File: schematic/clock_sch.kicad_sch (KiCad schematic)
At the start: 7 parts

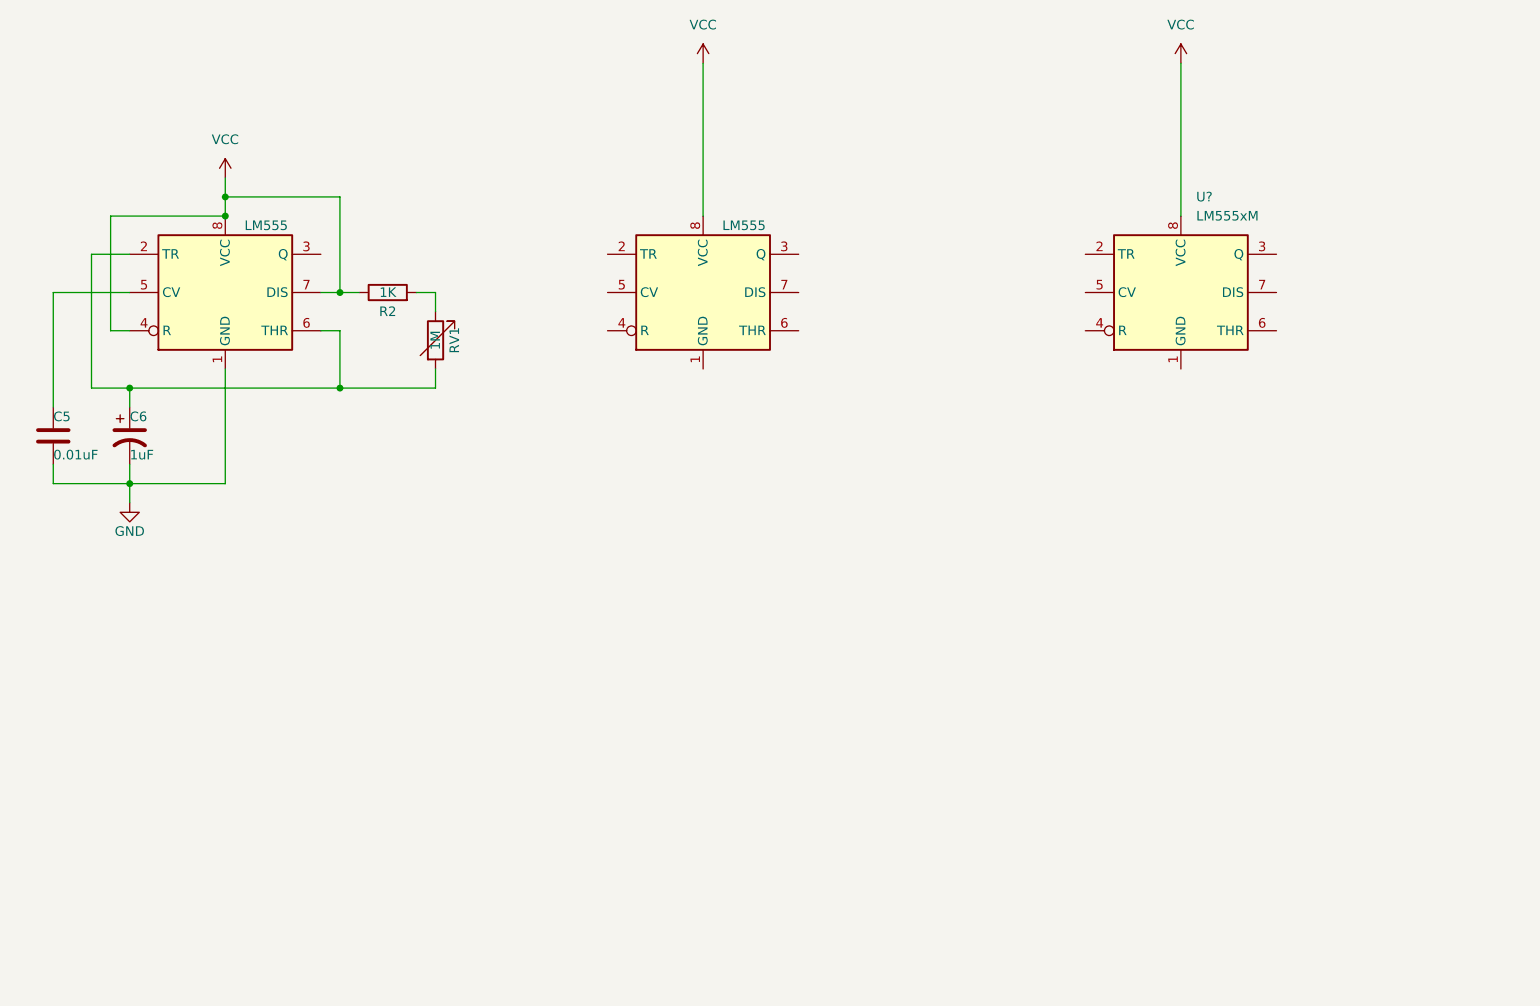
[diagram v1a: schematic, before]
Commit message: Added label and box
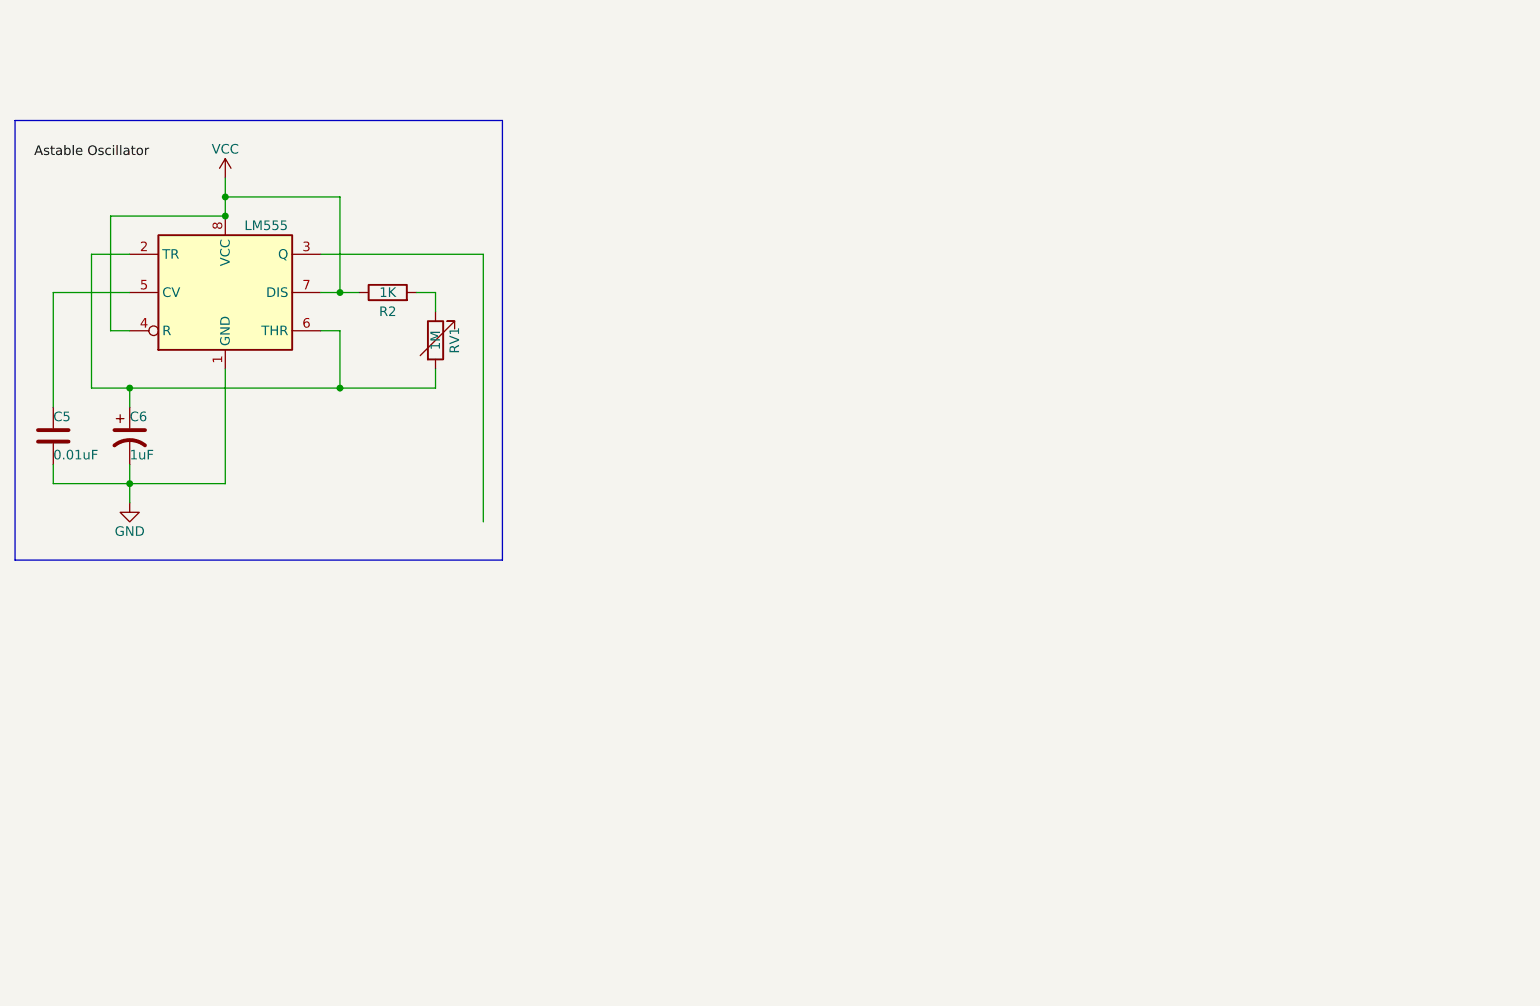
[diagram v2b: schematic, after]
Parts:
- removed U?: LM555, Package_SO:SOIC-8_3.9x4.9mm_P1.27mm, symbol Timer:LM555xM
- removed U?: LM555xM, Package_SO:SOIC-8_3.9x4.9mm_P1.27mm, symbol Timer:LM555xM
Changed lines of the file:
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@@
   (junction (at 50.8 96.52) (diameter 0) (color 0 0 0 0)
+  )
+  (wire (pts (xy 97.79 66.04) (xy 97.79 101.6))
+    (stroke (width 0) (type default) (color 0 0 0 0))
   )
   (wire (pts (xy 63.5 60.96) (xy 48.26 60.96))
@@
     (stroke (width 0) (type default) (color 0 0 0 0))
   )
-  (wire (pts (xy 190.5 40.64) (xy 190.5 60.96))
+  (polyline (pts (xy 100.33 106.68) (xy 100.33 48.26))
+    (stroke (width 0) (type default) (color 0 0 0 0))
+  )
+  (polyline (pts (xy 35.56 48.26) (xy 100.33 48.26))
     (stroke (width 0) (type default) (color 0 0 0 0))
   )
@@
     (stroke (width 0) (type default) (color 0 0 0 0))
   )
+  (polyline (pts (xy 35.56 106.68) (xy 100.33 106.68))
+    (stroke (width 0) (type default) (color 0 0 0 0))
+  )
   (wire (pts (xy 76.2 76.2) (xy 78.74 76.2))
+    (stroke (width 0) (type default) (color 0 0 0 0))
+  )
+  (polyline (pts (xy 35.56 48.26) (xy 35.56 106.68))
     (stroke (width 0) (type default) (color 0 0 0 0))
   )
@@
   )
   (wire (pts (xy 63.5 58.42) (xy 78.74 58.42))
-    (stroke (width 0) (type default) (color 0 0 0 0))
-  )
-  (wire (pts (xy 127 40.64) (xy 127 60.96))
     (stroke (width 0) (type default) (color 0 0 0 0))
   )
@@
     (stroke (width 0) (type default) (color 0 0 0 0))
   )
-  (symbol (lib_id "Timer:LM555xM") (at 127 71.12 0) (unit 1)
-    (in_bom yes) (on_board yes)
-    (property "Reference" "U?" (id 0) (at 129.0194 58.42 0)
-      (effects (font (size 1.27 1.27)) (justify left) hide)
-    )
-    (property "Value" "LM555" (id 1) (at 129.54 62.23 0)
-      (effects (font (size 1.27 1.27)) (justify left))
-    )
-    (property "Footprint" "Package_SO:SOIC-8_3.9x4.9mm_P1.27mm" (id 2) (at 148.59 81.28 0)
-      (effects (font (size 1.27 1.27)) hide)
-    )
-    (property "Datasheet" "http://www.ti.com/lit/ds/symlink/lm555.pdf" (id 3) (at 148.59 81.28 0)
-      (effects (font (size 1.27 1.27)) hide)
-    )
-    (pin "1")
-    (pin "8")
-    (pin "2")
-    (pin "3")
-    (pin "4")
-    (pin "5")
-    (pin "6")
-    (pin "7")
+  (wire (pts (xy 76.2 66.04) (xy 97.79 66.04))
+    (stroke (width 0) (type default) (color 0 0 0 0))
+  )
+  (label "Astable Oscillator" (at 38.1 53.34 0)
+    (effects (font (size 1.27 1.27)) (justify left bottom))
   )
   (symbol (lib_id "Timer:LM555xM") (at 63.5 71.12 0) (unit 1)
@@
     (pin "6")
     (pin "7")
-  )
-  (symbol (lib_id "Timer:LM555xM") (at 190.5 71.12 0) (unit 1)
-    (in_bom yes) (on_board yes) (fields_autoplaced)
-    (property "Reference" "U?" (id 0) (at 192.5194 58.42 0)
-      (effects (font (size 1.27 1.27)) (justify left))
-    )
-    (property "Value" "LM555xM" (id 1) (at 192.5194 60.96 0)
-      (effects (font (size 1.27 1.27)) (justify left))
-    )
-    (property "Footprint" "Package_SO:SOIC-8_3.9x4.9mm_P1.27mm" (id 2) (at 212.09 81.28 0)
-      (effects (font (size 1.27 1.27)) hide)
-    )
-    (property "Datasheet" "http://www.ti.com/lit/ds/symlink/lm555.pdf" (id 3) (at 212.09 81.28 0)
-      (effects (font (size 1.27 1.27)) hide)
-    )
-    (pin "1")
-    (pin "8")
-    (pin "2")
-    (pin "3")
-    (pin "4")
-    (pin "5")
-    (pin "6")
-    (pin "7")
-  )
-  (symbol (lib_id "power:VCC") (at 190.5 40.64 0) (unit 1)
-    (in_bom yes) (on_board yes) (fields_autoplaced)
-    (property "Reference" "#PWR?" (id 0) (at 190.5 44.45 0)
-      (effects (font (size 1.27 1.27)) hide)
-    )
-    (property "Value" "VCC" (id 1) (at 190.5 35.56 0))
-    (property "Footprint" "" (id 2) (at 190.5 40.64 0)
-      (effects (font (size 1.27 1.27)) hide)
-    )
-    (property "Datasheet" "" (id 3) (at 190.5 40.64 0)
-      (effects (font (size 1.27 1.27)) hide)
-    )
-    (pin "1")
-  )
-  (symbol (lib_id "power:VCC") (at 127 40.64 0) (unit 1)
-    (in_bom yes) (on_board yes) (fields_autoplaced)
-    (property "Reference" "#PWR?" (id 0) (at 127 44.45 0)
-      (effects (font (size 1.27 1.27)) hide)
-    )
-    (property "Value" "VCC" (id 1) (at 127 35.56 0))
-    (property "Footprint" "" (id 2) (at 127 40.64 0)
-      (effects (font (size 1.27 1.27)) hide)
-    )
-    (property "Datasheet" "" (id 3) (at 127 40.64 0)
-      (effects (font (size 1.27 1.27)) hide)
-    )
-    (pin "1")
   )
   (symbol (lib_id "Device:R_Variable") (at 91.44 77.47 0) (unit 1)
@@
   )
   (symbol (lib_id "power:VCC") (at 63.5 55.88 0) (unit 1)
-    (in_bom yes) (on_board yes) (fields_autoplaced)
+    (in_bom yes) (on_board yes)
     (property "Reference" "#PWR?" (id 0) (at 63.5 59.69 0)
       (effects (font (size 1.27 1.27)) hide)
     )
-    (property "Value" "VCC" (id 1) (at 63.5 50.8 0))
+    (property "Value" "VCC" (id 1) (at 63.5 52.07 0))
     (property "Footprint" "" (id 2) (at 63.5 55.88 0)
       (effects (font (size 1.27 1.27)) hide)

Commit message: dded Monostable oscillator and mode selection circuits
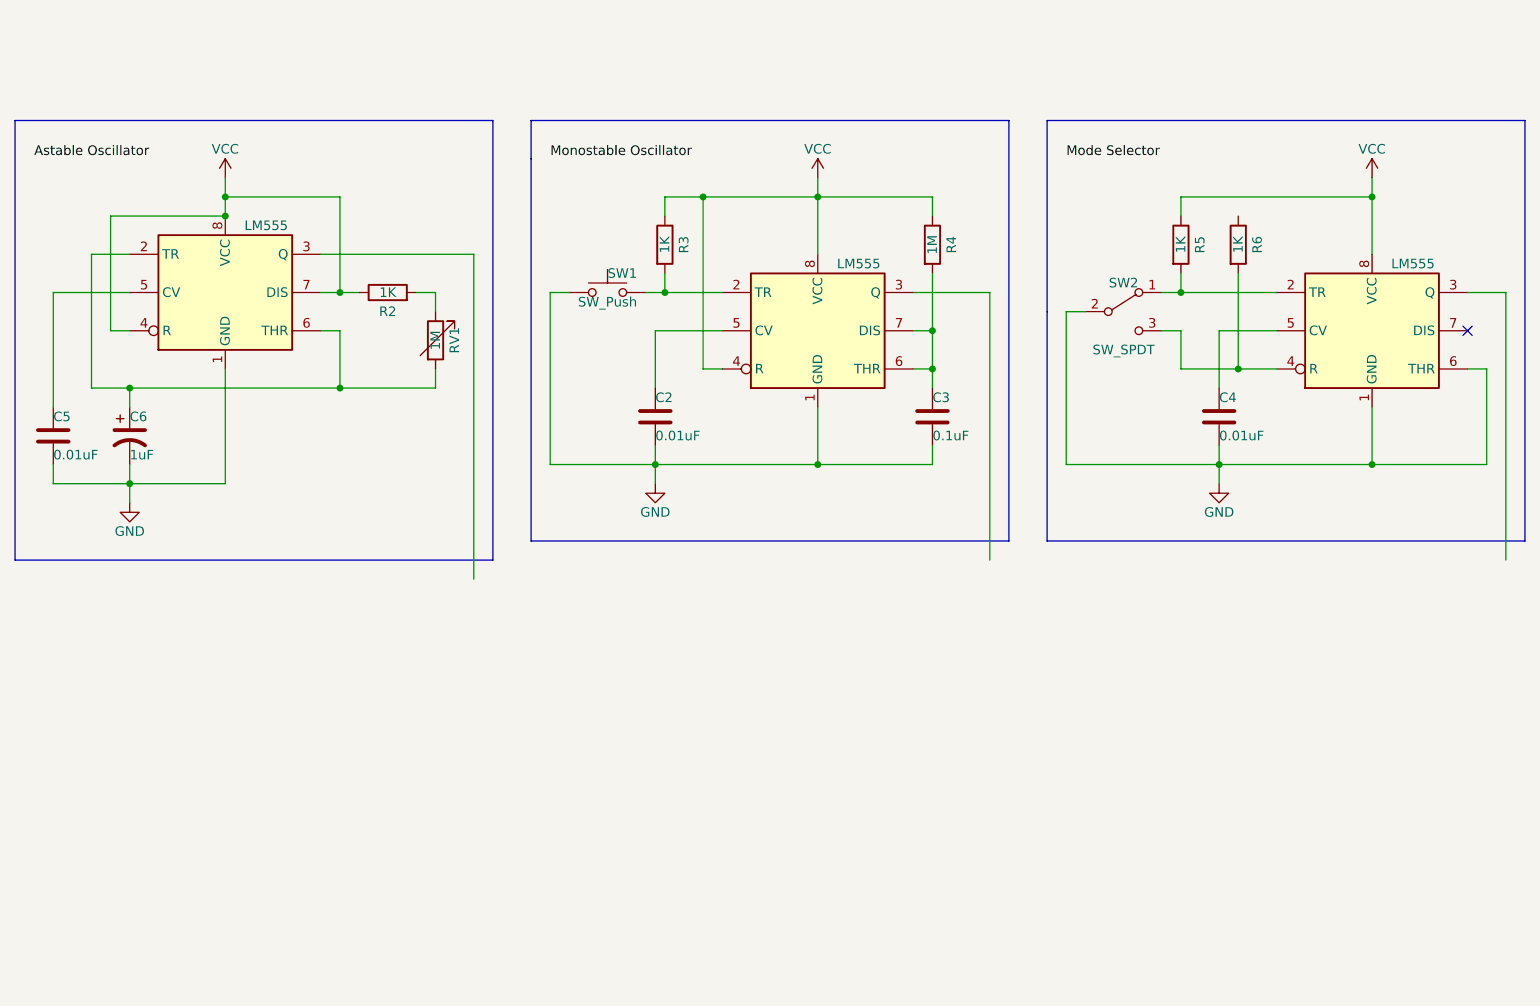
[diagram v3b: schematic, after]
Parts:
- added C2, C4: 0.01uF, symbol Device:C
- added C3: 0.1uF, symbol Device:C
- added R3, R5, R6: 1K, symbol Device:R
- added R4: 1M, symbol Device:R
- added SW1: SW_Push, symbol Switch:SW_Push
- added SW2: SW_SPDT, symbol Switch:SW_SPDT
- added U? (x2): LM555, Package_SO:SOIC-8_3.9x4.9mm_P1.27mm, symbol Timer:LM555xM
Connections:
- net GND: now also C2.2, C3.2, C4.2, SW1.1, SW2.2 (B), U?.1 (GND), U?.1 (GND), U?.6 (THR)
- net VCC: now also R3.1, R4.1, R5.1, U?.4 (R), U?.8 (VCC), U?.8 (VCC)
- new net: C2.1, U?.5 (CV)
- new net: R3.2, SW1.2, U?.2 (TR)
- new net: C4.1, U?.5 (CV)
- new net: R5.2, SW2.1 (A), U?.2 (TR)
- new net: R6.2, SW2.3 (C), U?.4 (R)
- new net: C3.1, R4.2, U?.6 (THR), U?.7 (DIS)
- no-connect marks 0 -> 1

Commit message: Implemented switching logic
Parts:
- added U4: 74LS04, symbol 74xx:74LS04
- added U5: 74LS08, symbol 74xx:74LS08
- added U6: 74LS32, symbol 74xx:74LS32
- gave numbers to parts that had none: 3
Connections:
- new net: U4.13, U5.8
- new net: U4.2, U5.4
- new net: U5.6, U6.2
- new net: U5.3, U6.1
- new net: U5.9, U6.3
- new net: U4.8, U5.10
